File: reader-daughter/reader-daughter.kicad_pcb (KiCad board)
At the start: 2 copper layers, 43.6 x 49.6 mm, 22 parts, among them J1 Conn_01x10_Female, J2 Conn_01x10_Female, J3 Conn_01x03_Male, J5 Conn_01x19_Female, J6 Conn_01x19_Female, J7 Conn_01x08_Male, T1 AO3400A

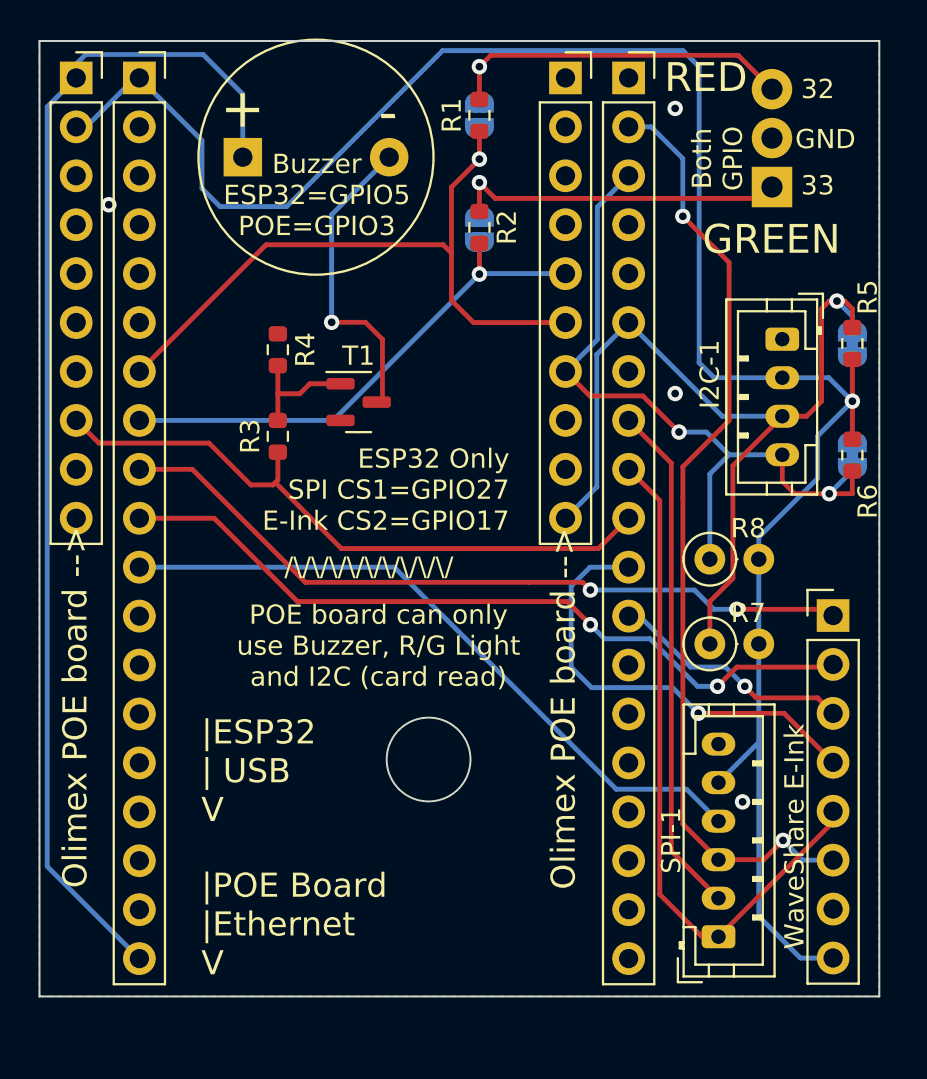
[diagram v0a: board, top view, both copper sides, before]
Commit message: updated boards with improved silkscreen and pad-shapes
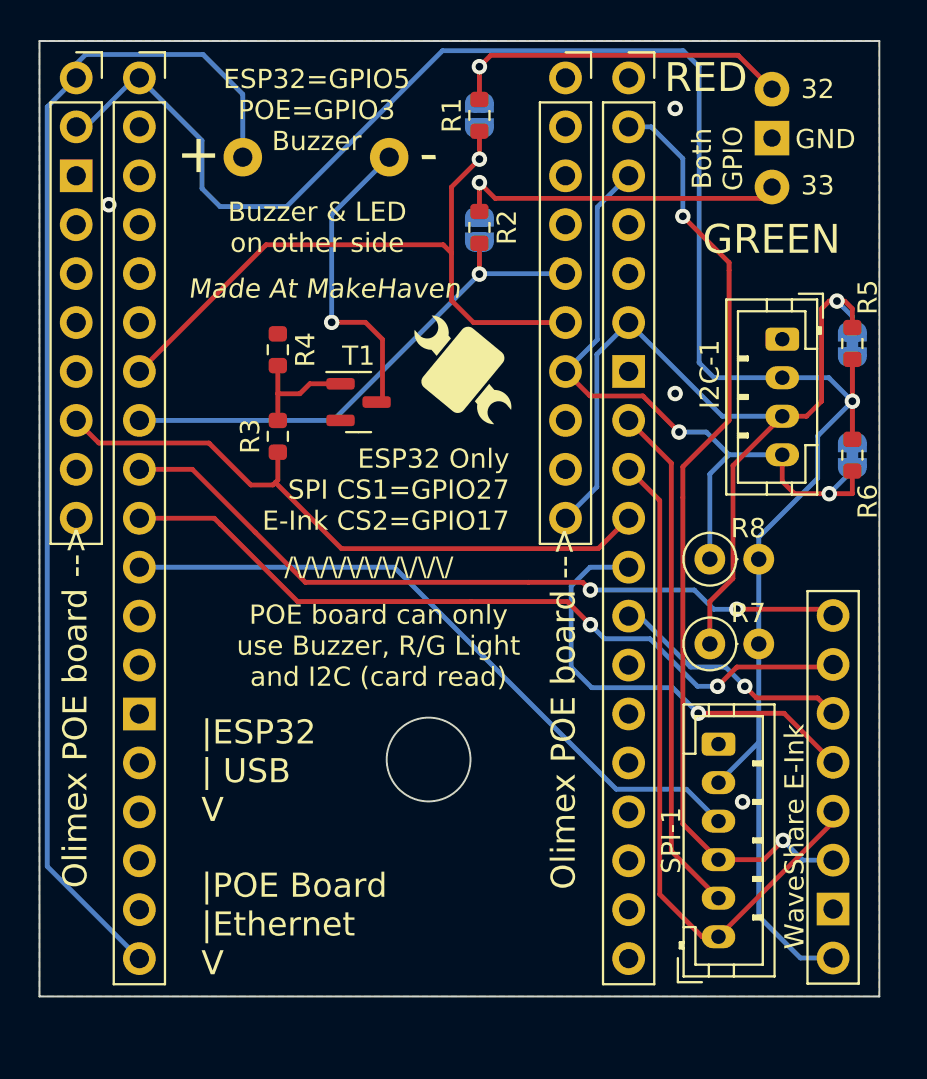
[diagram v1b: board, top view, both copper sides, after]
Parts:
- BZ1: moved to B.Cu
- J3: footprint TerminalBlock_TE-Connectivity:TerminalBlock_TE_282834-3_1x03_P2.54mm_Horizontal -> LED_THT:LED_D5.0mm-3; moved to B.Cu
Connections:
- JP1 pad 2: Net-(J3-Pad3) -> Net-(JP1-Pad2)
- JP2 pad 2: Net-(J3-Pad1) -> Net-(JP2-Pad2)
- R1 pad 2: Net-(J3-Pad3) -> Net-(JP1-Pad2)
- R2 pad 1: Net-(J3-Pad1) -> Net-(JP2-Pad2)
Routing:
- net Net-(JP1-Pad2): track 0.00 -> 19.7 mm, vias 0 -> 1
- net Net-(J3-Pad3): track 19.7 -> 0.00 mm, vias 1 -> 0
- net Net-(JP2-Pad2): track 0.00 -> 19.1 mm, vias 0 -> 1
- net Net-(J3-Pad1): track 19.1 -> 0.00 mm, vias 1 -> 0
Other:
- board text added: "'ESP32'=ESP32DevKitCV4+"
- board text added: "Buzzer & LED on other side"
- board text added: "ESP32=GPIO5 POE=GPIO3 Buzzer"
- board text added: "Made At MakeHaven"
- board text removed: "'ESP32' = ESP32 RevC"
